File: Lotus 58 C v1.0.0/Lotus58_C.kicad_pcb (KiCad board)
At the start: 2 copper layers, 139.1 x 107.7 mm, 137 parts, among them J1 USB_C_Receptacle_USB2.0, J2 Conn_01x02, J3 USB_C_Receptacle_USB2.0, P1 OLED, Q1 AO3401A, SW1 Kailh hotswap MX socket, SW10 Kailh hotswap MX socket, SW11 Kailh hotswap MX socket, SW12 Kailh hotswap MX socket, SW13 Kailh hotswap MX socket, SW14 Kailh hotswap MX socket, SW15 Kailh hotswap MX socket, SW16 Kailh hotswap MX socket, SW17 Kailh hotswap MX socket, SW18 Kailh hotswap MX socket, SW19 Kailh hotswap MX socket, SW2 Kailh hotswap MX socket, SW20 Kailh hotswap MX socket, SW21 Kailh hotswap MX socket, SW22 Kailh hotswap MX socket, SW23 Kailh hotswap MX socket, SW24 Kailh hotswap MX socket, SW25 Kailh hotswap MX socket, SW26 Kailh hotswap MX socket, SW27 Kailh hotswap MX socket, SW28 Kailh hotswap MX socket, SW29 Kailh hotswap MX socket, SW3 Kailh hotswap MX socket, SW30 Rotary_Encoder_Switch, SW31 Rotary_Encoder_Switch, SW4 Kailh hotswap MX socket, SW5 Kailh hotswap MX socket, SW6 Kailh hotswap MX socket, SW7 Kailh hotswap MX socket, SW8 Kailh hotswap MX socket, SW9 Kailh hotswap MX socket, U1 ProMicro, U2 SRV05-4

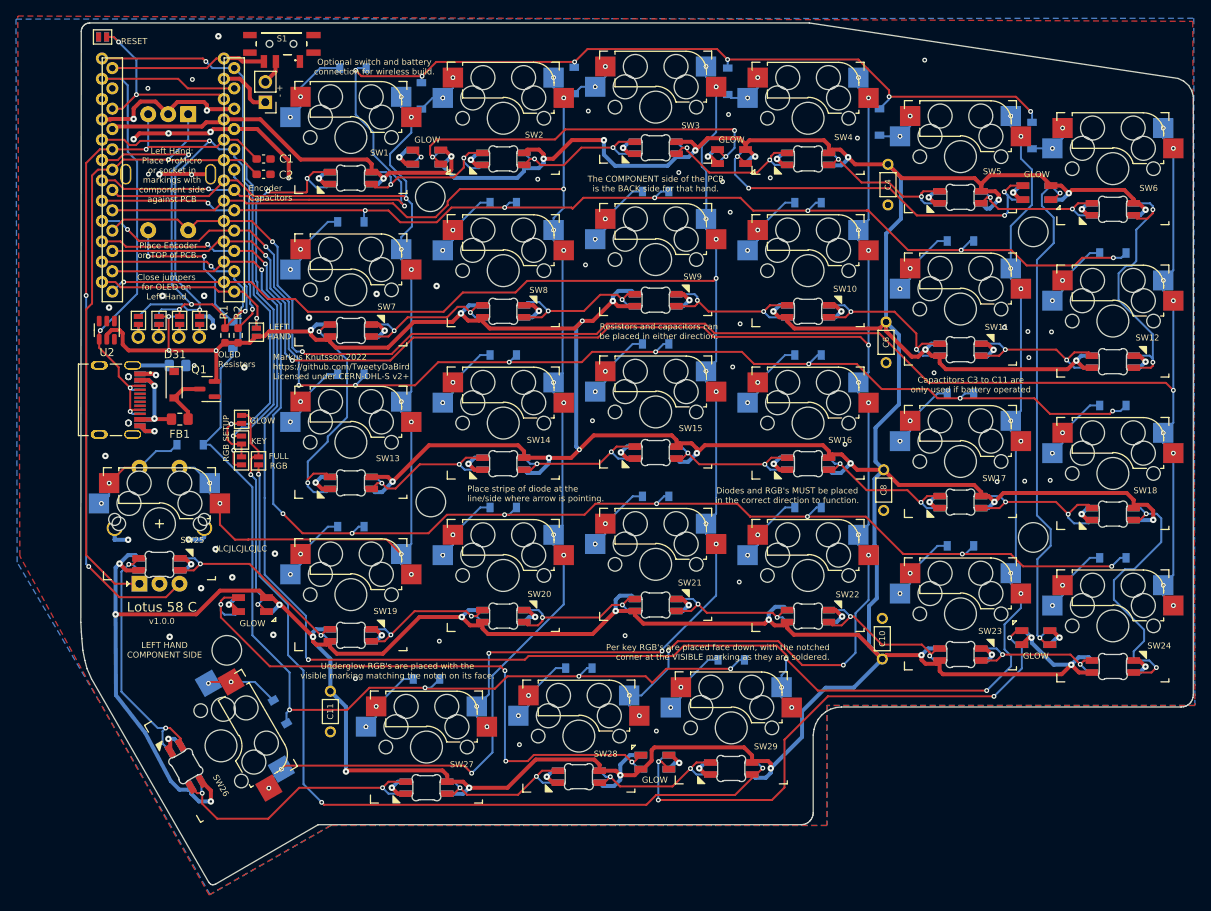
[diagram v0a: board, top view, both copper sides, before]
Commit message: Lotus C
Minor tweaks
SMD capacitors
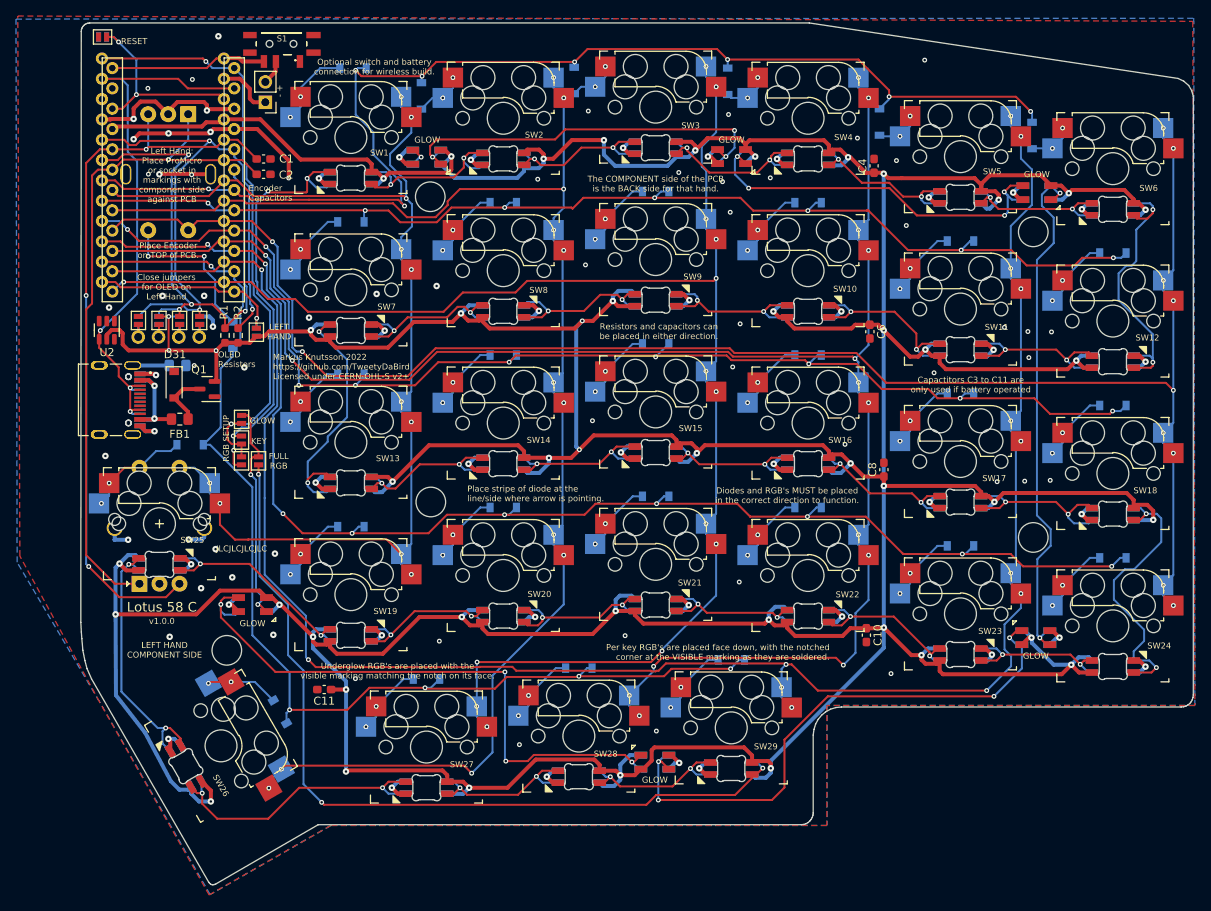
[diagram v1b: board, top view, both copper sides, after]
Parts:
- C10, C11, C4, C6, C8: footprint Common Library:RESISTOR_Reversible -> Capacitor_SMD:C_0603_1608Metric_Pad1.08x0.95mm_HandSolder
- moved C4 2.92 mm to (179.8, 53.5), turned to 90 degrees
- moved C11 2.86 mm to (111.1, 119.0), turned to 180 degrees
- moved C8 2.56 mm to (181.0, 91.5), turned to 90 degrees
- moved C6 2.42 mm to (179.3, 74.3)
- moved C10 2.04 mm to (178.8, 112.2), turned to -90 degrees
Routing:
- net VCC: track 875.9 -> 869.5 mm, vias 42 -> 47
- net col2: track 223.2 -> 219.3 mm
- net col1: track 245.2 -> 243.6 mm
- net row4: track 145.8 -> 145.1 mm
- net GND: vias 96 -> 99
